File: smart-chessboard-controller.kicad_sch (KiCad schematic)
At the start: 59 parts, among them J1 USB_C_Receptacle_USB2.0, J2 Micro_SD_Card_Det_Hirose_DM3C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, J3 Conn_02x03_Odd_Even, J4 Conn_01x12_MountingPin, J5 NX3224T024, J8 Conn_01x05, J9 Conn_01x05, Q1 S8050, Q2 S8050, SW2 SW_SPST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

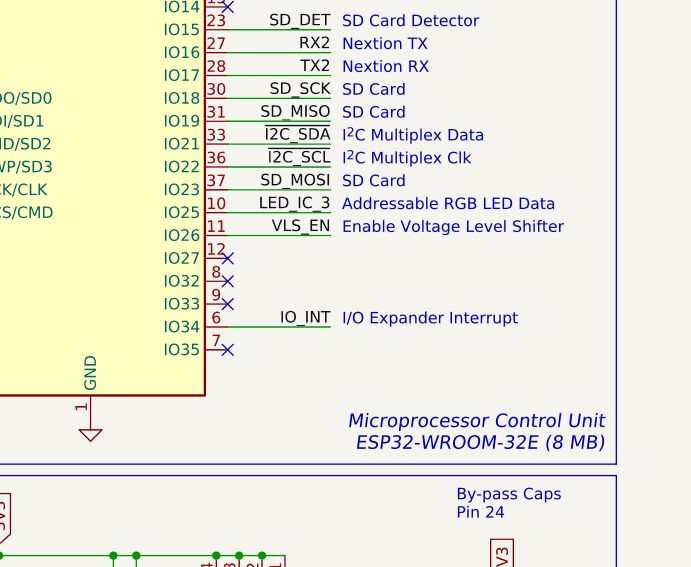
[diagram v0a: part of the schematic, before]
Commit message: change pin assignment for io_int
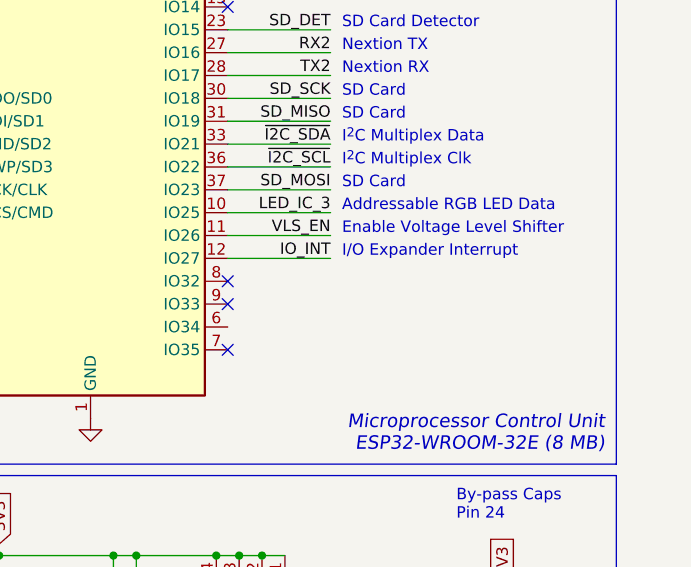
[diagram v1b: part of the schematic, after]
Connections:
- net IO_INT: now also U2.12 (IO27); no longer U2.6 (IO34)
- no-connect marks 47 -> 46
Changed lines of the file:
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@@
   (no_connect (at 267.97 57.15))
   (no_connect (at 283.21 128.27))
-  (no_connect (at 298.45 74.93))
   (no_connect (at 298.45 80.01))
   (no_connect (at 298.45 85.09))
@@
     (stroke (width 0) (type default) (color 0 0 0 0))
   )
-  (wire (pts (xy 298.45 82.55) (xy 309.88 82.55))
+  (wire (pts (xy 298.45 74.93) (xy 309.88 74.93))
     (stroke (width 0) (type default) (color 0 0 0 0))
   )
@@
     (effects (font (size 1.27 1.27)) (justify left bottom))
   )
-  (text "I/O Expander Interrupt" (at 311.15 82.55 0)
+  (text "I/O Expander Interrupt" (at 311.15 74.93 0)
     (effects (font (size 1.27 1.27)) (justify left bottom))
   )
@@
     (effects (font (size 1.27 1.27)) (justify right bottom))
   )
-  (label "IO_INT" (at 309.88 82.55 180)
-    (effects (font (size 1.27 1.27)) (justify right bottom))
-  )
+  (label "IO_INT" (at 309.88 74.93 180)
+    (effects (font (size 1.27 1.27)) (justify right bottom))
+  )

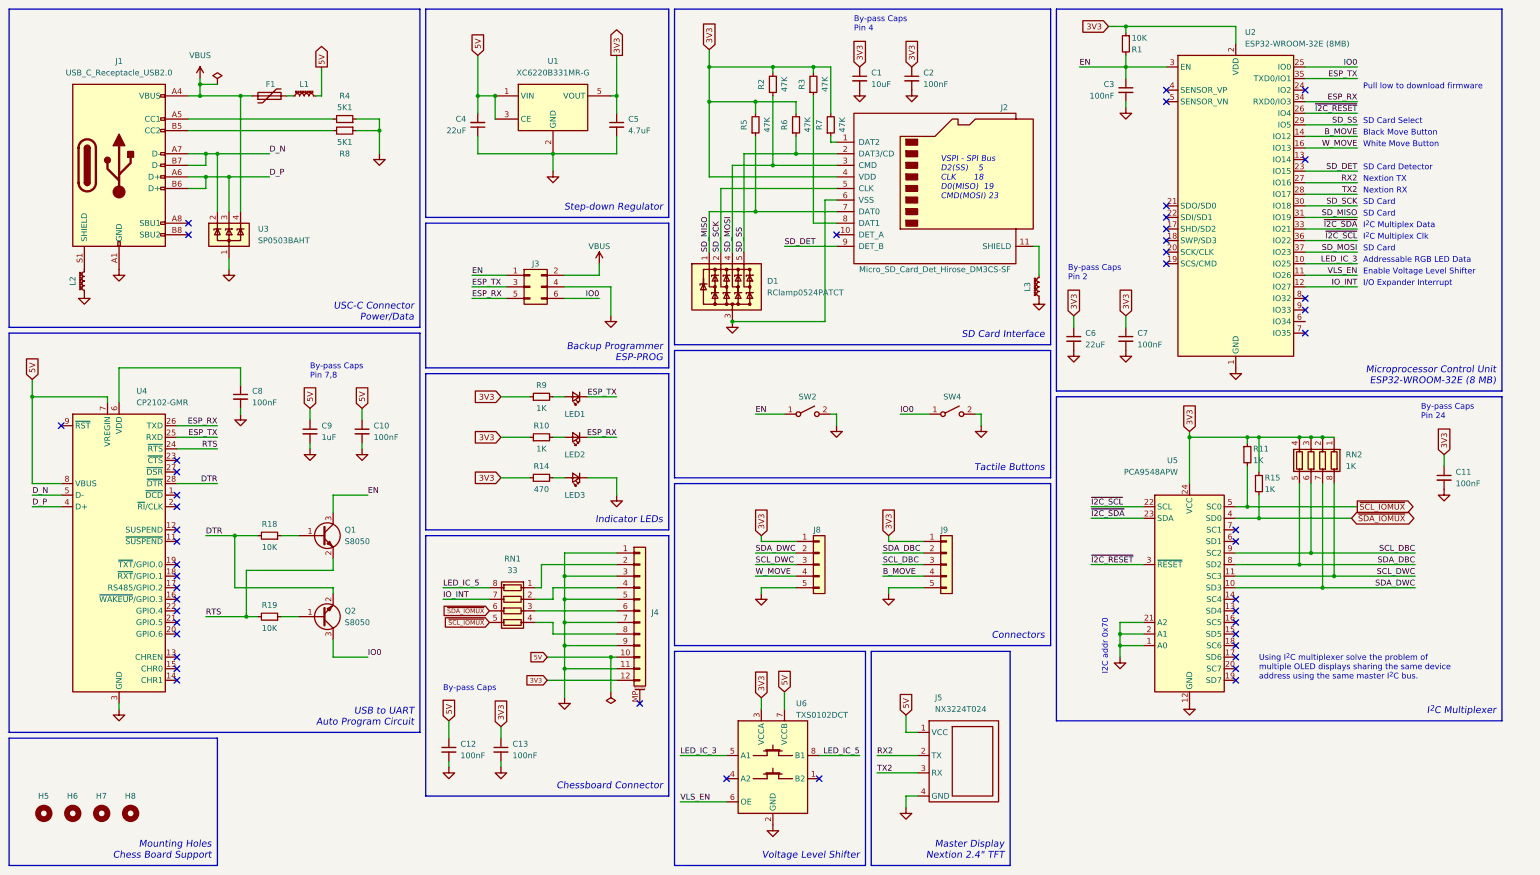
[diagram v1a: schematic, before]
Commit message: add bypass caps
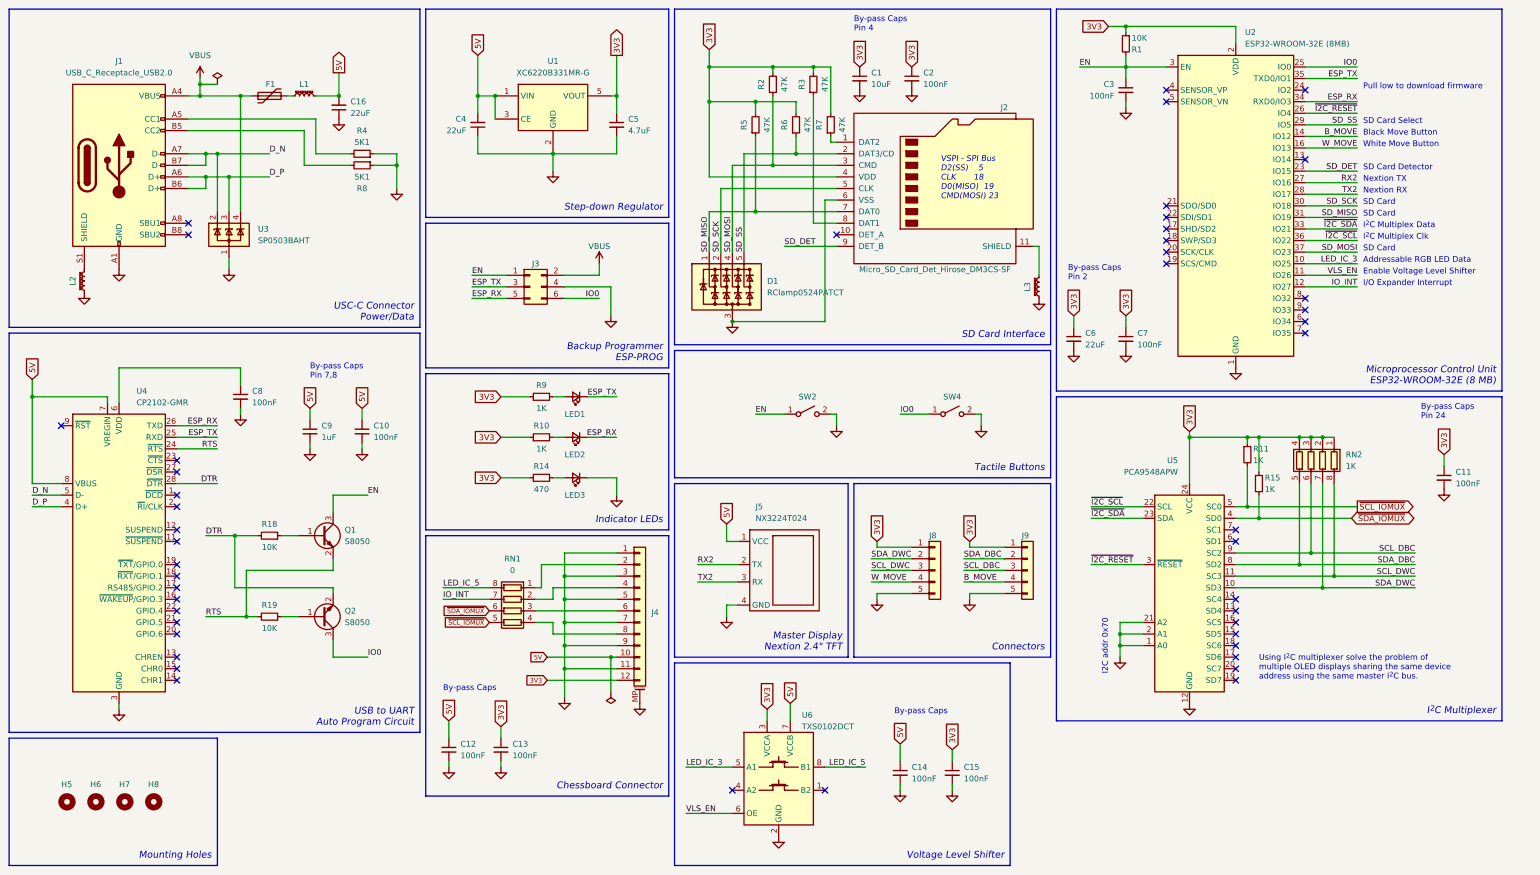
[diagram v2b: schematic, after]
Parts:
- added C14, C15: 100nF, Capacitor_SMD:C_0603_1608Metric, symbol Device:C_Small
- added C16: 22uF, Capacitor_SMD:C_0603_1608Metric, symbol Device:C_Small
- RN1: value 33 -> 0; LCSC C169805 -> (none)
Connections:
- net 3V3: now also C15.1
- net 5V: now also C14.1, C16.2
- net GND: now also J4.MP (MountPin), C14.2, C15.2, C16.1
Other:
- note added: "Mounting Holes"
- note removed: "Mounting Holes Chess Board Support"
- moved on the sheet: H5, H6, H7, H8, J5, J8, J9, R4, R8, U6

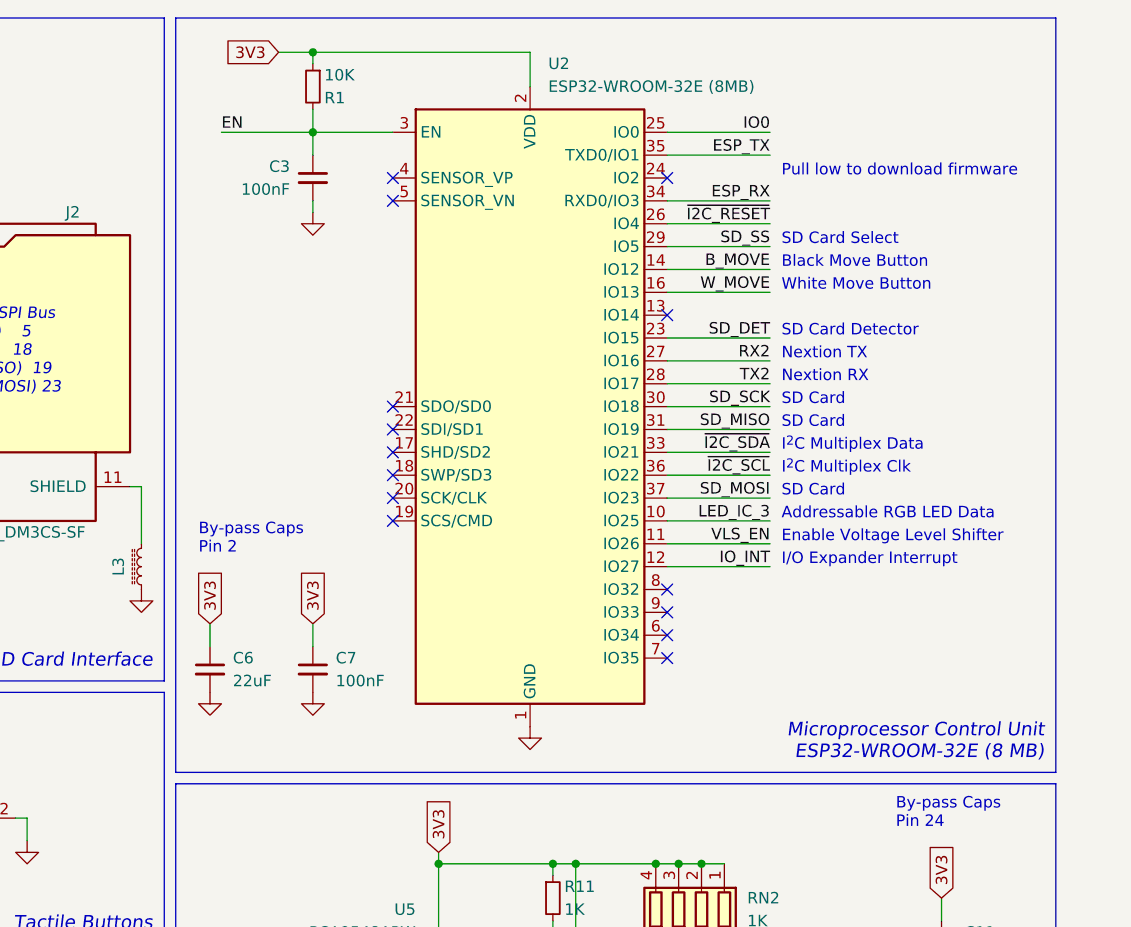
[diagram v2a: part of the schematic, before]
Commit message: update design to use ESP32 WROVER module
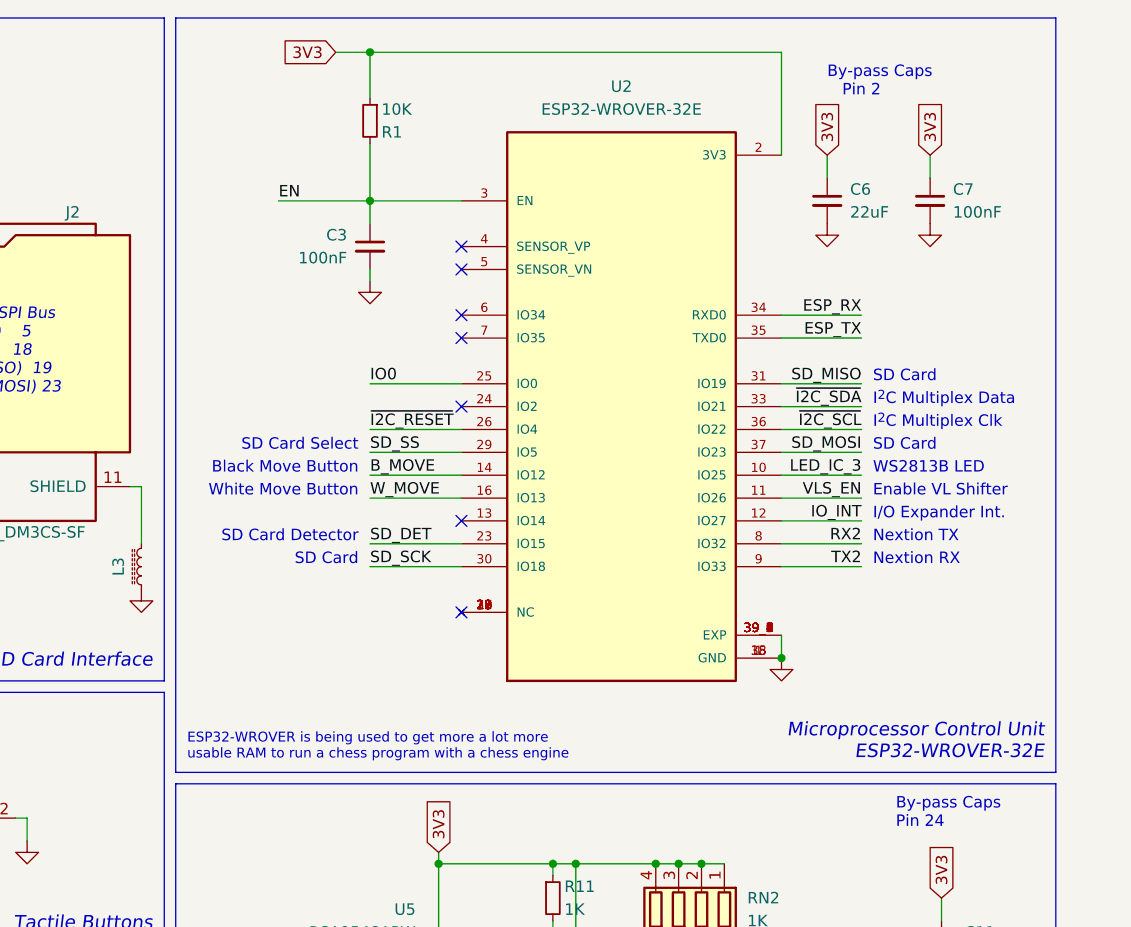
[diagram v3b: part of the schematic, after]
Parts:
- U2: value ESP32-WROOM-32E (8MB) -> ESP32-WROVER-32E; footprint RF_Module:ESP32-WROOM-32 -> User Custom Footprint:XCVR_ESP32-WROVER-E-N4R8; symbol RF_Module:ESP32-WROOM-32D -> User_Symbols:ESP32-WROVER-E-N4R8; LCSC C701342 -> C2973667; MANUFACTURER (none) -> Espressif Systems; MAXIMUM_PACKAGE_HEIGHT (none) -> 3.45 mm; PARTREV (none) -> 1.6; SNAPEDA_PN (none) -> ESP32-WROVER-E-N4R8; STANDARD (none) -> Manufacturer Recommendations
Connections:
- net GND: now also U2.39_1 (EXP), U2.39_2 (EXP), U2.39_3 (EXP), U2.39_4 (EXP), U2.39_5 (EXP), U2.39_6 (EXP), U2.39_7 (EXP), U2.39_8 (EXP), U2.39_9 (EXP); no longer U2.39 (GND)
- net RX2: now also U2.8 (IO32); no longer U2.27 (IO16)
- net TX2: now also U2.9 (IO33); no longer U2.28 (IO17)
- net at U2.17 (NC): now also U2.18 (NC), U2.19 (NC), U2.20 (NC), U2.21 (NC), U2.22 (NC), U2.27 (NC), U2.28 (NC), U2.32 (NC)
- no-connect marks 46 -> 39
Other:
- note added: "ESP32-WROVER is being used to get more a lot more usable RAM to run a chess program with a chess engine"
- note added: "Enable VL Shifter"
- note added: "I/O Expander Int."
- note added: "Microprocessor Control Unit ESP32-WROVER-32E"
- note added: "WS2813B LED"
- note removed: "Addressable RGB LED Data"
- note removed: "Enable Voltage Level Shifter"
- note removed: "I/O Expander Interrupt"
- note removed: "Microprocessor Control Unit ESP32-WROOM-32E (8 MB)"
- note removed: "Pull low to download firmware"
- moved on the sheet: C3, C6, C7, R1
